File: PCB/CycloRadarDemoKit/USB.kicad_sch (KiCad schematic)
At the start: 41 parts, among them J301 USB_C_Receptacle_USB2.0, Q301 L8050QLT1G, Q302 L8050QLT1G, U301 CP2102N-Axx-xQFN28

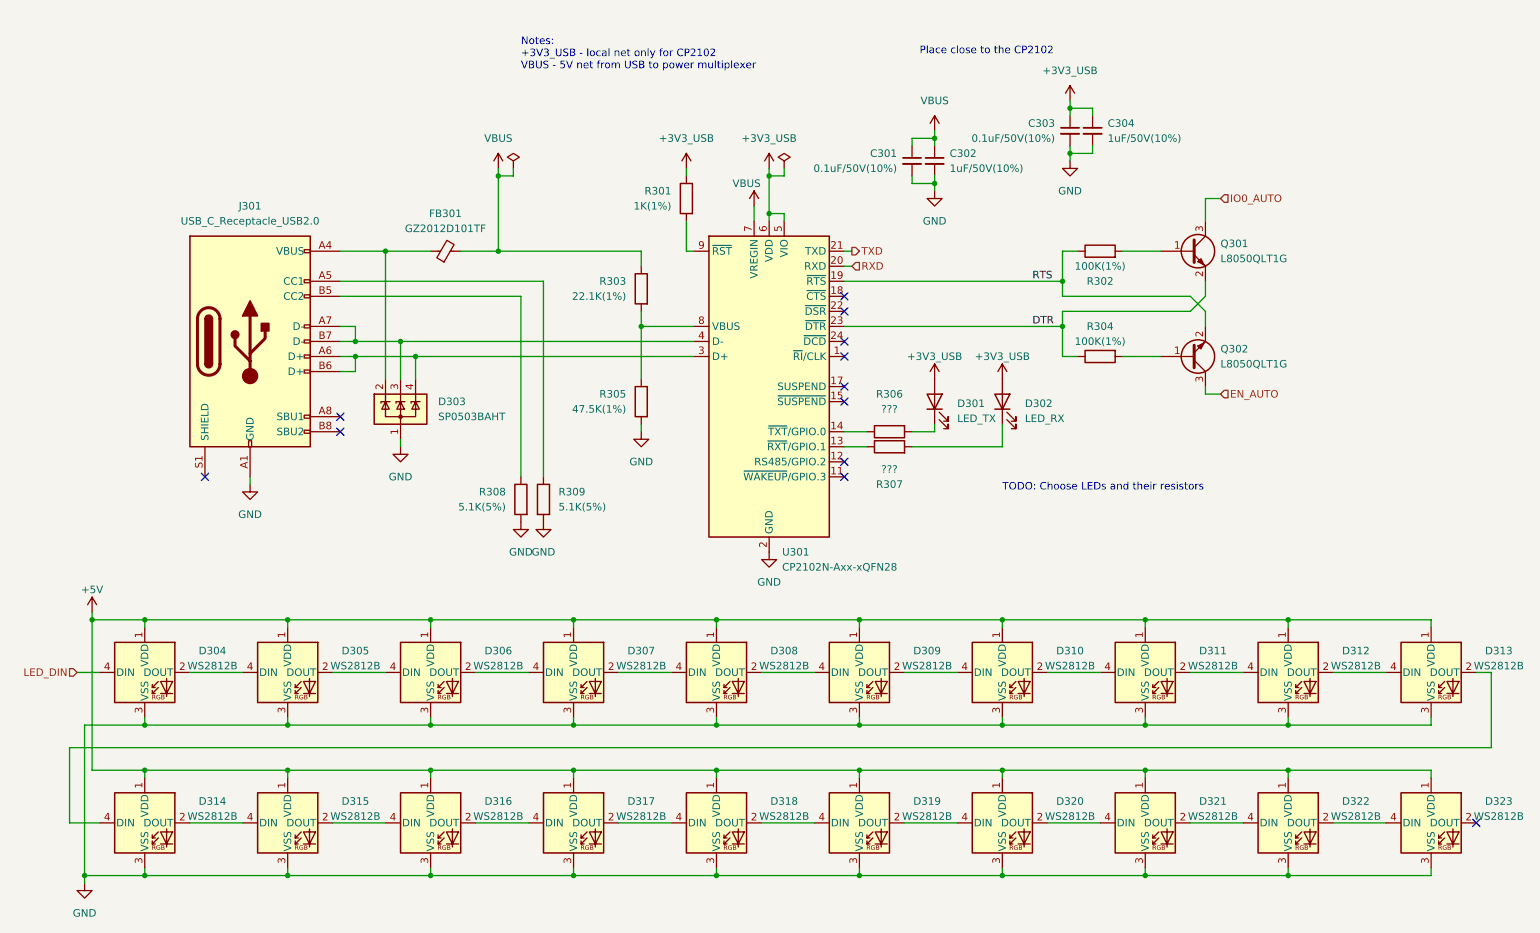
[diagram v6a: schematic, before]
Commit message: MPU added, power managemennt updated
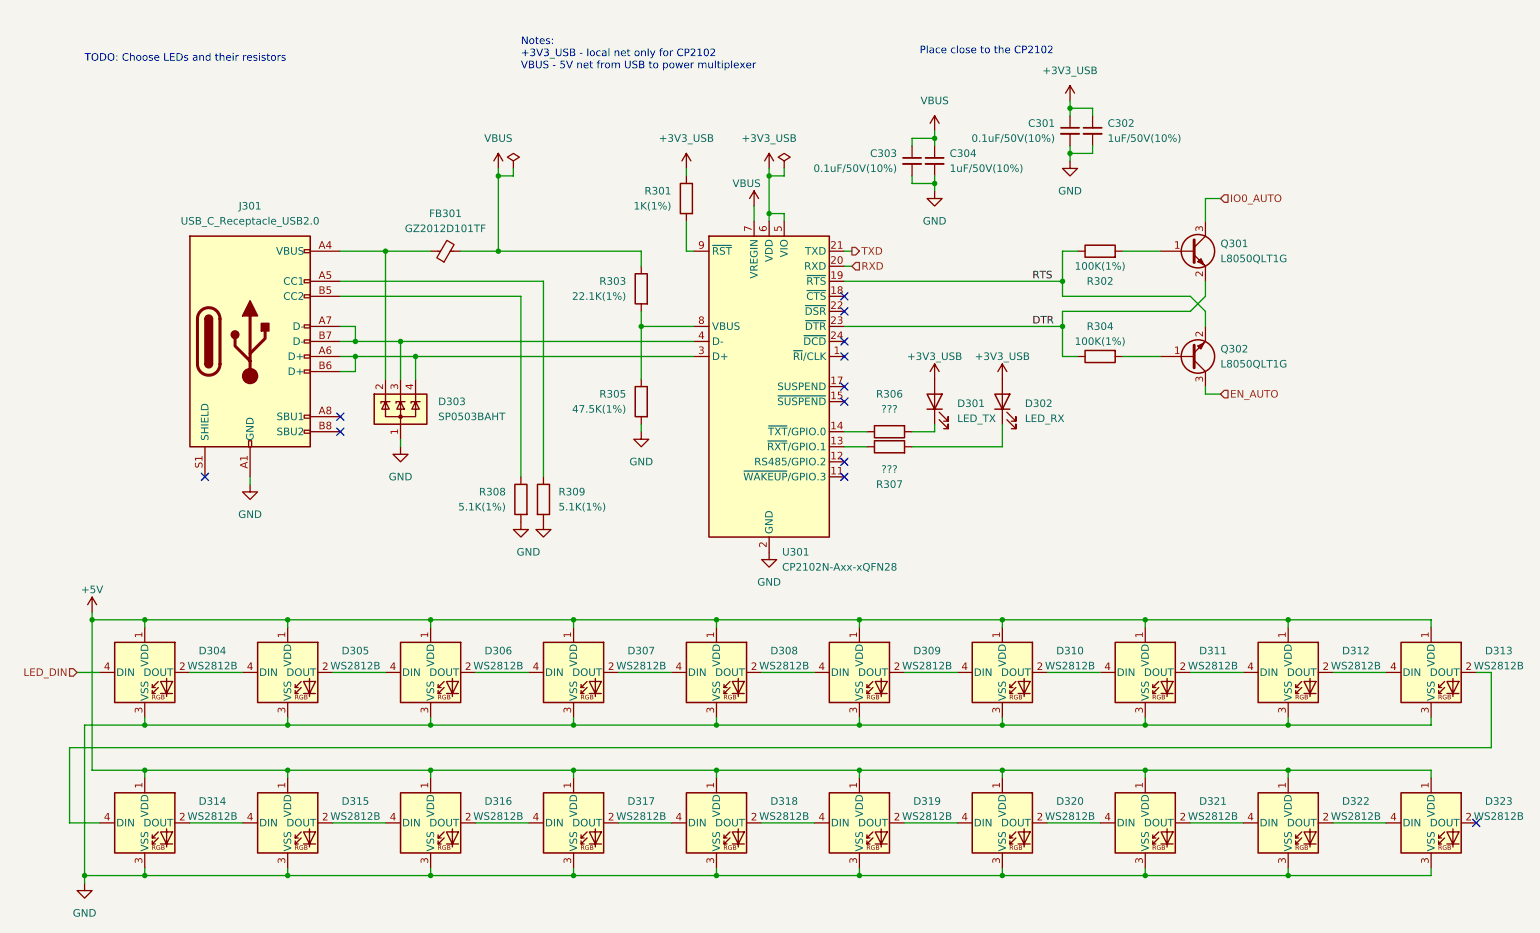
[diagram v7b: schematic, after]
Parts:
- R308, R309: value 5.1K(5%) -> 5.1K(1%); footprint (none) -> Resistor_SMD:R_0603_1608Metric; LCSC (none) -> C23186
- renumbered C303 to C301, C304 to C302, C301 to C303, C302 to C304

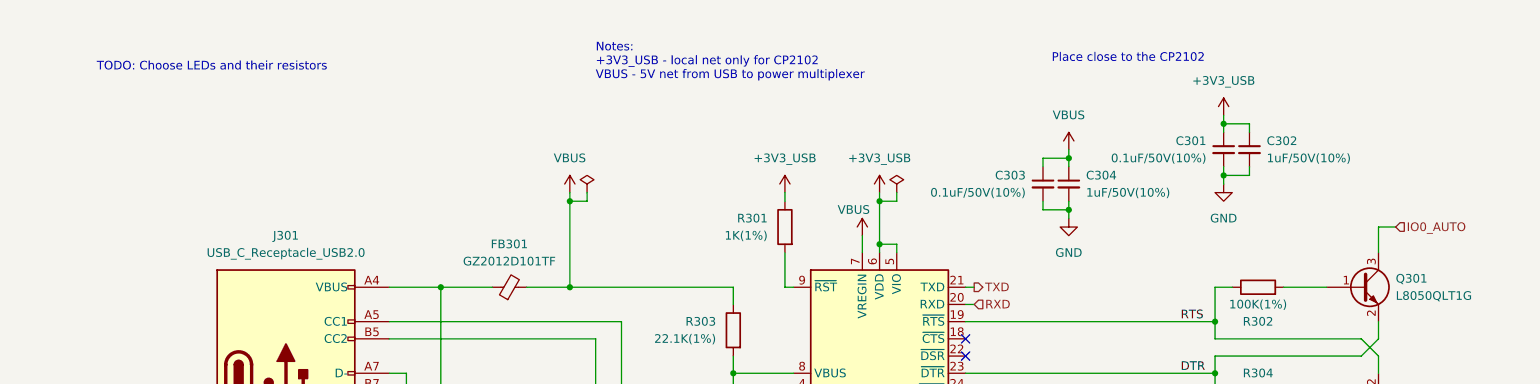
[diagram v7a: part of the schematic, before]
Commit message: added buzzer and pins for Radar
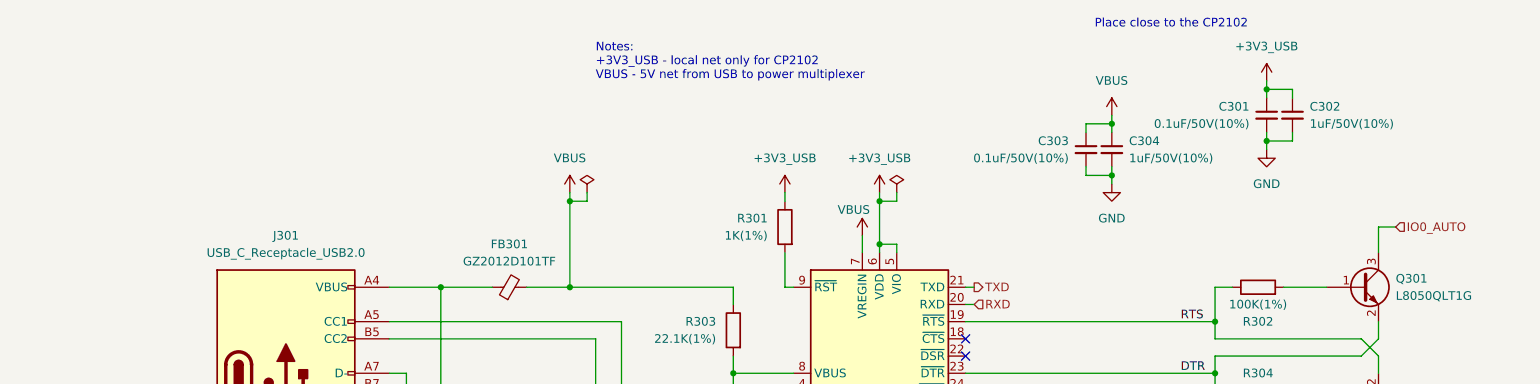
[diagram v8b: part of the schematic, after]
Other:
- note removed: "TODO: Choose LEDs and their resistors"
- moved on the sheet: C301, C302, C303, C304
